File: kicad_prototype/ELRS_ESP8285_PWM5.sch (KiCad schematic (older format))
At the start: 48 parts, among them J1 Conn_Coaxial, J2 Conn_01x05, J3 Conn_01x05, J4 Conn_01x05, J5 Conn_Coaxial, U1 SPX3819M5-L-3-3, U2 ESP8285, U5 2450FM07D0034T, U6 SX1281, Y2 26M, Y3 52M

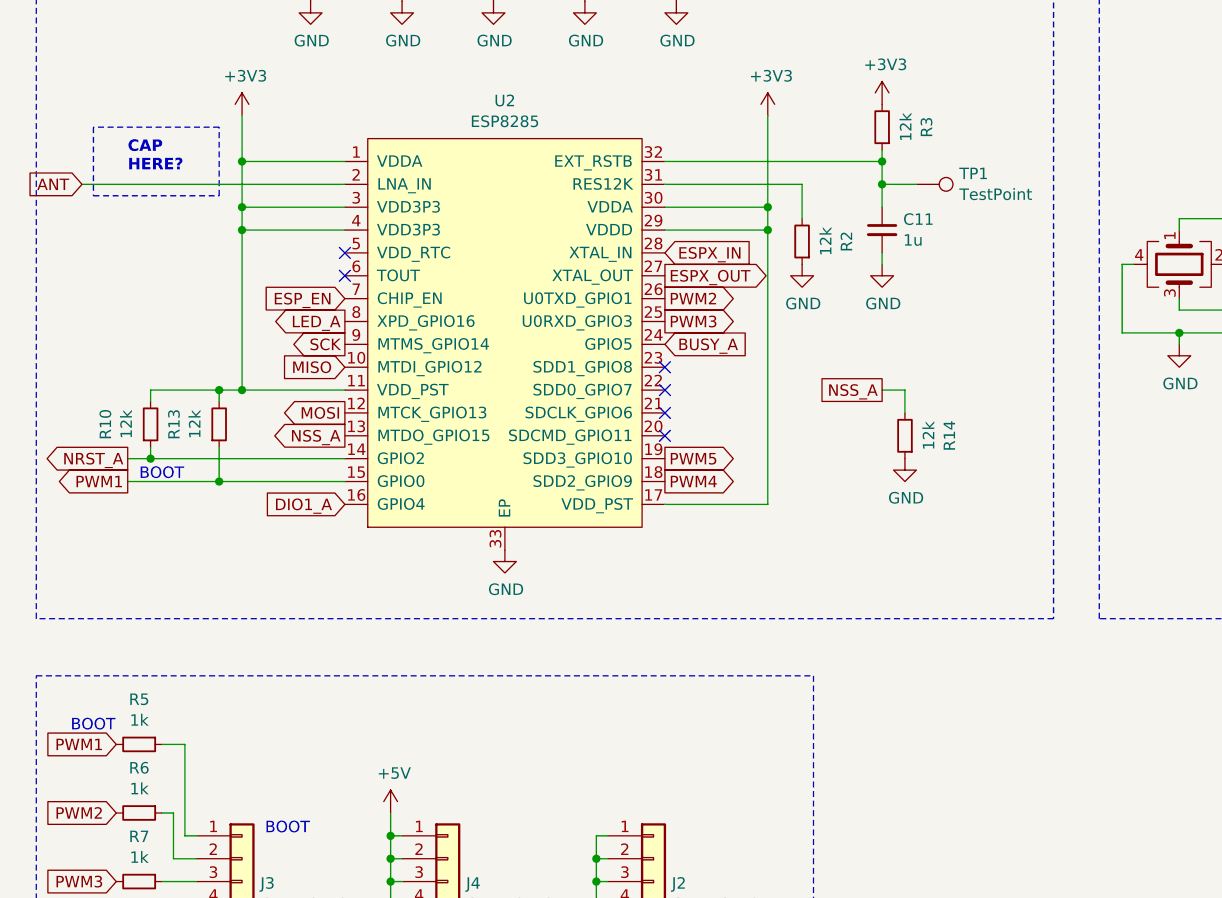
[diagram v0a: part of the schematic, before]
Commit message: move pogo pad to boot input, minor layout changes
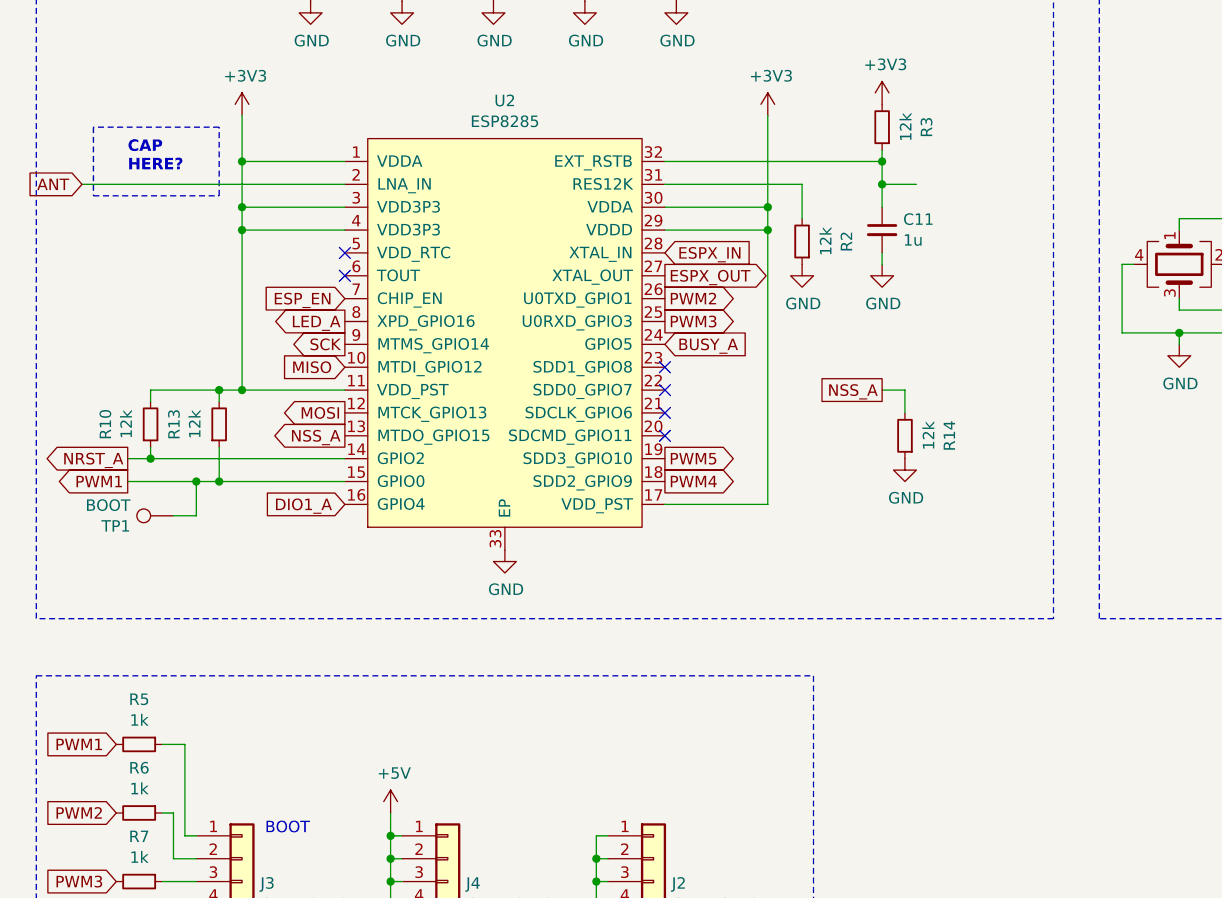
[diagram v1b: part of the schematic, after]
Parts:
- TP1: value TestPoint -> BOOT
- U2: footprint Package_DFN_QFN:QFN-32-1EP_5x5mm_P0.5mm_EP3.7x3.7mm -> ELRS_ESP8285_PWM5:QFN-32-1EP_5x5mm_P0.5mm_EP3.7x3.7mm_dense
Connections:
- net PWM1: now also TP1.1
- net at C11.1, R3.1, U2.32 (EXT_RSTB): no longer TP1.1
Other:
- moved on the sheet: TP1
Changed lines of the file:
@@
 Title "ELRS ESP8285 5xPWM"
 Date "2021-10-29"
-Rev "work in progress "
+Rev "work in progress"
 Comp "crteensy"
-Comment1 "crteensy"
+Comment1 ""
 Comment2 ""
 Comment3 ""
@@
 F 0 "U2" H 2700 5515 50  0000 C CNN
 F 1 "ESP8285" H 2700 5424 50  0000 C CNN
-F 2 "Package_DFN_QFN:QFN-32-1EP_5x5mm_P0.5mm_EP3.7x3.7mm" H 2700 4900 50  0001 C CNN
+F 2 "ELRS_ESP8285_PWM5:QFN-32-1EP_5x5mm_P0.5mm_EP3.7x3.7mm_dense" H 2700 4900 50  0001 C CNN
 F 3 "" H 2700 4900 50  0001 C CNN
 	1    2700 4500
@@
 	1    0    0    -1
 $EndComp
-Text Notes 1100 5150 0    50   ~ 0
-BOOT
 Text GLabel 1050 5150 0    50   Output ~ 0
 PWM1
@@
 L Connector:TestPoint TP1
 U 1 1 61AB1B8D
-P 4500 3850
-F 0 "TP1" V 4454 4038 50  0000 L CNN
-F 1 "TestPoint" V 4545 4038 50  0000 L CNN
-F 2 "TestPoint:TestPoint_Pad_D1.0mm" H 4700 3850 50  0001 C CNN
-F 3 "~" H 4700 3850 50  0001 C CNN
-	1    4500 3850
-	0    1    1    0
+P 1250 5300
+F 0 "TP1" V 1204 5488 50  0000 L CNN
+F 1 "BOOT" V 1295 5488 50  0000 L CNN
+F 2 "TestPoint:TestPoint_Pad_D1.0mm" H 1450 5300 50  0001 C CNN
+F 3 "~" H 1450 5300 50  0001 C CNN
+	1    1250 5300
+	0    -1   -1   0
 $EndComp
 $Comp
@@
 	1450 5150 2000 5150
 Wire Wire Line
-	1050 5150 1450 5150
+	1050 5150 1350 5150
 Connection ~ 1450 5150
 $Comp
@@
 Wire Wire Line
 	4350 4750 4450 4750
-Text Notes 800  6250 0    50   ~ 0
-BOOT
 Text Notes 1650 6700 0    50   ~ 0
 BOOT
+Wire Wire Line
+	1250 5300 1350 5300
+Wire Wire Line
+	1350 5300 1350 5150
+Connection ~ 1350 5150
+Wire Wire Line
+	1350 5150 1450 5150
 $EndSCHEMATC

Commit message: schematic/layout rev0.3
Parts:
- added C12: 100n, Capacitor_SMD:C_0402_1005Metric, symbol Device:C_Small
- added J6: Conn_01x02, Connector_PinHeader_2.54mm:PinHeader_1x02_P2.54mm_Vertical, symbol Connector_Generic:Conn_01x02
- added JP1: 6S4S, Jumper:SolderJumper-2_P1.3mm_Bridged_RoundedPad1.0x1.5mm, symbol Jumper:SolderJumper_2_Bridged
- added R15: 24k, Resistor_SMD:R_0402_1005Metric, symbol Device:R_Small
- added R16: 1k, Resistor_SMD:R_0402_1005Metric, symbol Device:R_Small
- added R17: 47k, Resistor_SMD:R_0402_1005Metric, symbol Device:R_Small
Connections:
- net GND: now also C12.2, J6.1 (Pin_1), R16.1
- net ADC_sig: now reaches U2.6 (TOUT)
- net ADC_sig: now also C12.1, JP1.2 (B), R15.1, R16.2
- new net: J6.2 (Pin_2), R15.2, R17.2
- new net: JP1.1 (A), R17.1
- no-connect marks 7 -> 6
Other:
- note added: "JP closed (default) for 6S\nCut open for 4S"
- moved on the sheet: C19, C20, C4, R1, Y2

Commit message: update rev0.6
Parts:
- added C13: 10p, Capacitor_SMD:C_0402_1005Metric, symbol Device:C_Small
- D1: value LED -> blue_2V9
- D2: value LED -> true_gr_3V3
- D4: value LED -> red_2V1
- JP1: value 6S4S -> 4S; footprint Jumper:SolderJumper-2_P1.3mm_Bridged_RoundedPad1.0x1.5mm -> Jumper:SolderJumper-2_P1.3mm_Open_RoundedPad1.0x1.5mm; symbol Jumper:SolderJumper_2_Bridged -> Jumper:SolderJumper_2_Open
- R11: value 560R -> 270R
- R12: value 3k9 -> 4k7
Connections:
- wire segments 171 -> 170
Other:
- note added: "JP open (default) for 6S\nClose for 4S"
- note removed: "CAP\nHERE?"
- note removed: "JP closed (default) for 6S\nCut open for 4S"
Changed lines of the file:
@@
 Sheet 1 1
 Title "ELRS ESP8285 5xPWM"
-Date "2021-11-01"
-Rev "rev 0.3"
+Date "2021-11-22"
+Rev "rev 0.6"
 Comp "crteensy"
 Comment1 ""
@@
 P 4700 1250
 F 0 "D1" V 4739 1132 50  0000 R CNN
-F 1 "LED" V 4648 1132 50  0000 R CNN
+F 1 "blue_2V9" V 4648 1132 50  0000 R CNN
 F 2 "LED_SMD:LED_0402_1005Metric" H 4700 1250 50  0001 C CNN
 F 3 "~" H 4700 1250 50  0001 C CNN
@@
 P 4700 1600
 F 0 "R11" V 4900 1600 50  0000 C CNN
-F 1 "560R" V 4800 1600 50  0000 C CNN
+F 1 "270R" V 4800 1600 50  0000 C CNN
 F 2 "Resistor_SMD:R_0402_1005Metric" H 4700 1600 50  0001 C CNN
 F 3 "~" H 4700 1600 50  0001 C CNN
@@
 P 1050 1550
 F 0 "D2" V 1089 1432 50  0000 R CNN
-F 1 "LED" V 998 1432 50  0000 R CNN
+F 1 "true_gr_3V3" V 998 1432 50  0000 R CNN
 F 2 "LED_SMD:LED_0402_1005Metric" H 1050 1550 50  0001 C CNN
 F 3 "~" H 1050 1550 50  0001 C CNN
@@
 P 1050 1200
 F 0 "R12" V 1250 1200 50  0000 C CNN
-F 1 "3k9" V 1150 1200 50  0000 C CNN
+F 1 "4k7" V 1150 1200 50  0000 C CNN
 F 2 "Resistor_SMD:R_0402_1005Metric" H 1050 1200 50  0001 C CNN
 F 3 "~" H 1050 1200 50  0001 C CNN
@@
 P 6400 2800
 F 0 "D4" V 6439 2682 50  0000 R CNN
-F 1 "LED" V 6348 2682 50  0000 R CNN
+F 1 "red_2V1" V 6348 2682 50  0000 R CNN
 F 2 "LED_SMD:LED_0402_1005Metric" H 6400 2800 50  0001 C CNN
 F 3 "~" H 6400 2800 50  0001 C CNN
@@
 Wire Wire Line
 	3400 3750 4350 3750
-Wire Wire Line
-	4350 3750 4350 3850
 $Comp
 L Connector:TestPoint TP1
@@
 Wire Wire Line
 	1450 4750 1150 4750
-Wire Wire Line
-	4500 3850 4350 3850
-Connection ~ 4350 3850
-Wire Wire Line
-	4350 3850 4350 3950
 $Comp
 L power:+3V3 #PWR0126
@@
 $EndComp
 Wire Wire Line
-	850  3850 2000 3850
-Wire Notes Line
-	900  3600 900  3900
-Wire Notes Line
-	900  3900 1450 3900
-Wire Notes Line
-	1450 3900 1450 3600
-Wire Notes Line
-	1450 3600 900  3600
-Text Notes 1050 3800 0    50   ~ 10
-CAP\nHERE?
+	850  3850 1100 3850
 $Comp
 L Connector:Conn_Coaxial J5
@@
 	6300 1550 6700 1550
 $Comp
-L Jumper:SolderJumper_2_Bridged JP1
+L Jumper:SolderJumper_2_Open JP1
 U 1 1 61A51B28
 P 6450 1100
 F 0 "JP1" H 6450 1305 50  0000 C CNN
-F 1 "6S4S" H 6450 1214 50  0000 C CNN
-F 2 "Jumper:SolderJumper-2_P1.3mm_Bridged_RoundedPad1.0x1.5mm" H 6450 1100 50  0001 C CNN
+F 1 "4S" H 6450 1214 50  0000 C CNN
+F 2 "Jumper:SolderJumper-2_P1.3mm_Open_RoundedPad1.0x1.5mm" H 6450 1100 50  0001 C CNN
 F 3 "~" H 6450 1100 50  0001 C CNN
 	1    6450 1100
@@
 	6700 1550 6900 1550
 Text Notes 6000 850  0    50   ~ 0
-JP closed (default) for 6S\nCut open for 4S
+JP open (default) for 6S\nClose for 4S
 Wire Notes Line
 	5950 650  5950 1200
@@
 Wire Notes Line
 	7050 650  5950 650
+$Comp
+L Device:C_Small C13
+U 1 1 61B221AE
+P 1200 3850
+F 0 "C13" H 1292 3896 50  0000 L CNN
+F 1 "10p" H 1292 3805 50  0000 L CNN
+F 2 "Capacitor_SMD:C_0402_1005Metric" H 1200 3850 50  0001 C CNN
+F 3 "~" H 1200 3850 50  0001 C CNN
+	1    1200 3850
+	0    -1   -1   0
+$EndComp
+Wire Wire Line
+	1300 3850 2000 3850
+Wire Wire Line
+	4350 3750 4350 3950
 $EndSCHEMATC
